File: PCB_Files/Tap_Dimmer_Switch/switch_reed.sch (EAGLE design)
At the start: 37 parts, among them P1 HT7333

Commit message: Added Design with additional reed (magnet) sensor
this version is not entirely finished and has to be improved upon
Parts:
- added C4, C6: 10nF, rcl:C-EUC0805
- added C7: 100u, rcl:CPOL-EUE5-8.5
- added R16, R17, R18, R19, R20, R22, R23, R25: 200k, rcl:R-EU_R0805
- added R21: 100k, rcl:R-EU_R0805
- added R24: 50k, rcl:R-EU_R0805
- added REED: (no value), jumper:JP1E
- added U$1, U$5, U$7: AO3401, diyHue:P-CH_AO3401
- added U$4, U$6, U$8: IRLML2502, diyHue:N-CH_IRLML2502
- C1: device rcl:C-EU025-025X050 -> rcl:C-EUC0805
- C2, C3: value 10nF -> 100u
- C5: value 100u -> 10u
- R1, R11, R12, R13, R14, R15, R2, R3, R4, R5, R8, R9: device diyHue:R-EU_MULTI -> rcl:R-EU_R0805
- R10: value 4k7 -> 10k; device diyHue:R-EU_MULTI -> rcl:R-EU_R0805
- R6, R7: value 100k -> 200k; device diyHue:R-EU_MULTI -> rcl:R-EU_R0805
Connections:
- removed net N$9: R15.1, U2.RX
- new net ADC: R23.1, R24.2, U2.ADC
- new net ESP_RX: R15.1, R21.1, R25.2, U2.RX
- new net N$11: C6.1, R19.2, U$1.D, U$5.G
- new net N$12: C4.1, R16.2, U$5.D
- new net N$13: C4.2, R17.2, U$4.G
- new net N$14: C6.2, R18.2, U$6.G
- new net N$16: R20.2, U$7.G, U$8.D
- new net N$17: R23.2, U$7.D
- new net N$18: R21.2, REED.1, U$1.G
- net +3V3: no longer R1.2, U$2.S
- net +5V: now also C7.+, R1.2, R20.1, REED.2, U$1.S, U$2.S, U$5.S, U$7.S
- net GND: now also C7.-, R16.1, R17.1, R18.1, R19.1, R22.1, R24.1, R25.1, U$4.S, U$6.S, U$8.S
- net GP0: now also R22.2, U$8.G
- net GP13: now also BTN5.D, R13.2; no longer BTN4.D, R5.2
- net GP14: now also BTN2.D, R3.2; no longer BTN5.D, R13.2
- net GP5: now also BTN4.D, R5.2; no longer BTN2.D, R3.2
- net RST: now also U$4.D, U$6.D
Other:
- moved on the sheet: R8, R9

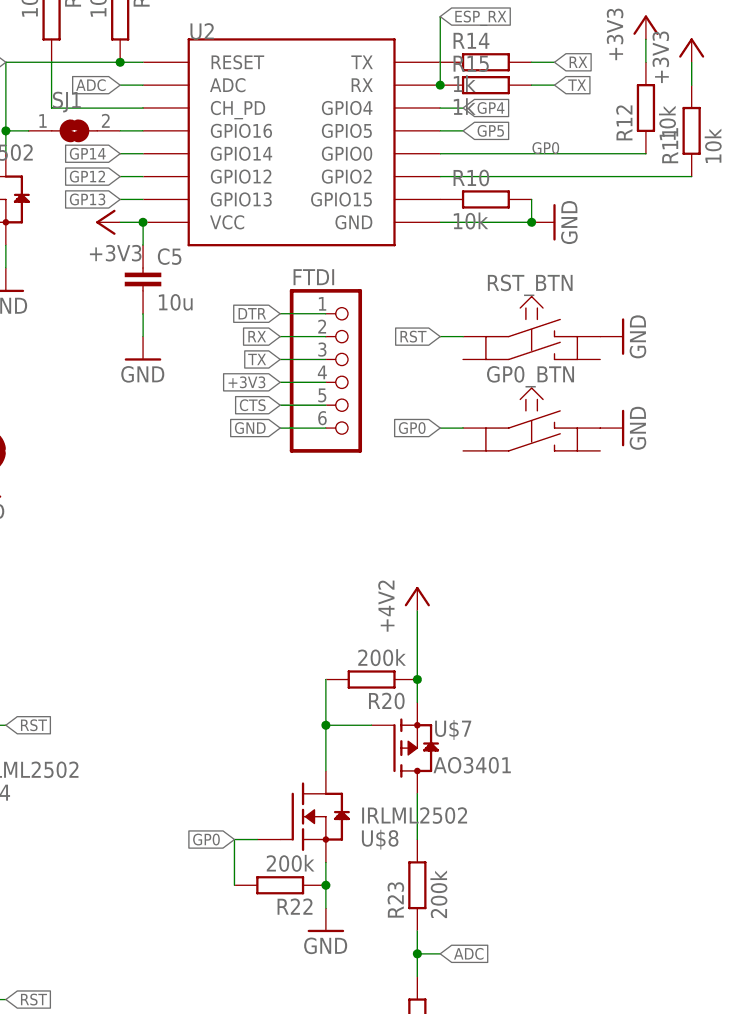
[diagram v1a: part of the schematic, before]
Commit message: created additional compact design of ws2812b module
this new design features smaller footprint, but the esp module ist partially outside the board, which will result in better wifi connection.

additionally the footprint of the HT7333 has been fixed as previously it had used the wrong package.
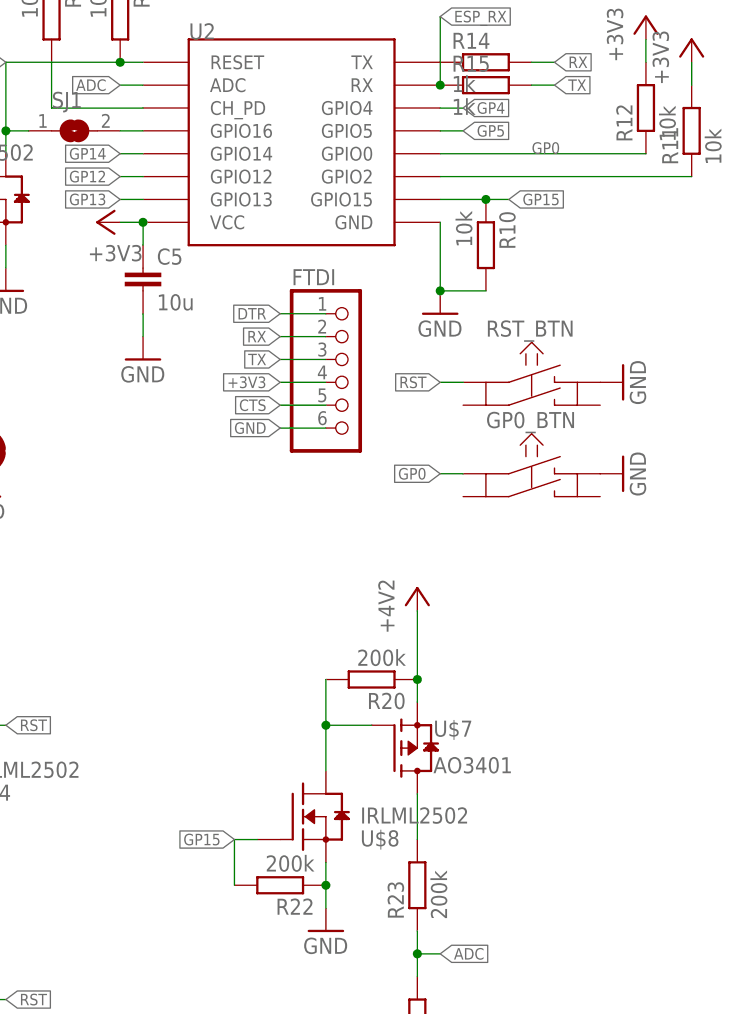
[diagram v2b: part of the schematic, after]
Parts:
- P1: device diyHue:HT7333 -> diyHue:HT7333SOT89
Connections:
- removed net N$4: R10.1, U2.GPIO15
- new net GP15: R10.1, R22.2, U$8.G, U2.GPIO15
- net GP0: no longer R22.2, U$8.G
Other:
- moved on the sheet: GP0_BTN, R10, RST_BTN
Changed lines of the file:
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@@
 <part name="C1" library="rcl" deviceset="C-EU" device="C0805" value="10nF"/>
 <part name="GND9" library="supply1" deviceset="GND" device=""/>
-<part name="P1" library="diyHue" deviceset="HT7333" device=""/>
+<part name="P1" library="diyHue" deviceset="HT7333" device="SOT89" value="HT7333"/>
 <part name="GND10" library="supply1" deviceset="GND" device=""/>
 <part name="FTDI" library="pinhead-2" deviceset="PINHD-1X06" device="_2.54-S"/>
@@
 <instance part="GND6" gate="1" x="83.82" y="0"/>
 <instance part="GND7" gate="1" x="96.52" y="0"/>
-<instance part="GND8" gate="1" x="167.64" y="15.24" rot="R90"/>
-<instance part="R10" gate="G$1" x="160.02" y="17.78"/>
+<instance part="GND8" gate="1" x="154.94" y="5.08"/>
+<instance part="R10" gate="G$1" x="160.02" y="12.7" rot="R270"/>
 <instance part="R11" gate="G$1" x="182.88" y="25.4" rot="R90"/>
 <instance part="R12" gate="G$1" x="177.8" y="27.94" rot="R90"/>
@@
 <instance part="C2" gate="G$1" x="68.58" y="45.72"/>
 <instance part="C3" gate="G$1" x="40.64" y="45.72"/>
-<instance part="RST_BTN" gate="G$1" x="165.1" y="0"/>
+<instance part="RST_BTN" gate="G$1" x="165.1" y="-5.08"/>
 <instance part="+3V4" gate="G$1" x="182.88" y="35.56"/>
-<instance part="GND11" gate="1" x="175.26" y="2.54" rot="R90"/>
-<instance part="GP0_BTN" gate="G$1" x="165.1" y="-10.16"/>
-<instance part="GND12" gate="1" x="175.26" y="-7.62" rot="R90"/>
+<instance part="GND11" gate="1" x="175.26" y="-2.54" rot="R90"/>
+<instance part="GP0_BTN" gate="G$1" x="165.1" y="-15.24"/>
+<instance part="GND12" gate="1" x="175.26" y="-12.7" rot="R90"/>
 <instance part="SJ1" gate="1" x="114.3" y="25.4"/>
 <instance part="R13" gate="G$1" x="66.04" y="2.54" rot="R90"/>
@@
 <pinref part="U2" gate="G$1" pin="GND"/>
 <pinref part="GND8" gate="1" pin="GND"/>
-<wire x1="165.1" y1="15.24" x2="154.94" y2="15.24" width="0.1524" layer="91"/>
+<wire x1="154.94" y1="7.62" x2="154.94" y2="15.24" width="0.1524" layer="91"/>
 <pinref part="R10" gate="G$1" pin="2"/>
-<wire x1="165.1" y1="17.78" x2="165.1" y2="15.24" width="0.1524" layer="91"/>
-<junction x="165.1" y="15.24"/>
+<wire x1="160.02" y1="7.62" x2="154.94" y2="7.62" width="0.1524" layer="91"/>
+<junction x="154.94" y="7.62"/>
 </segment>
 <segment>
@@
 <segment>
 <pinref part="RST_BTN" gate="G$1" pin="A"/>
-<wire x1="157.48" y1="2.54" x2="154.94" y2="2.54" width="0.1524" layer="91"/>
-<label x="154.94" y="2.54" size="1.27" layer="95" rot="R180" xref="yes"/>
+<wire x1="157.48" y1="-2.54" x2="154.94" y2="-2.54" width="0.1524" layer="91"/>
+<label x="154.94" y="-2.54" size="1.27" layer="95" rot="R180" xref="yes"/>
 </segment>
 <segment>
@@
 </segment>
 </net>
-<net name="N$4" class="0">
+<net name="GP15" class="0">
 <segment>
 <pinref part="U2" gate="G$1" pin="GPIO15"/>
 <pinref part="R10" gate="G$1" pin="1"/>
-</segment>
-</net>
-<net name="N$5" class="0">
-<segment>
-<pinref part="U2" gate="G$1" pin="GPIO2"/>
-<pinref part="R11" gate="G$1" pin="1"/>
-<wire x1="154.94" y1="20.32" x2="182.88" y2="20.32" width="0.1524" layer="91"/>
-</segment>
-</net>
-<net name="GP0" class="0">
-<segment>
-<pinref part="R12" gate="G$1" pin="1"/>
-<pinref part="U2" gate="G$1" pin="GPIO0"/>
-<wire x1="177.8" y1="22.86" x2="154.94" y2="22.86" width="0.1524" layer="91"/>
-<label x="165.1" y="22.86" size="1.27" layer="95"/>
-</segment>
-<segment>
-<pinref part="GP0_BTN" gate="G$1" pin="A"/>
-<wire x1="157.48" y1="-7.62" x2="154.94" y2="-7.62" width="0.1524" layer="91"/>
-<label x="154.94" y="-7.62" size="1.27" layer="95" rot="R180" xref="yes"/>
+<wire x1="160.02" y1="17.78" x2="162.56" y2="17.78" width="0.1524" layer="91"/>
+<junction x="160.02" y="17.78"/>
+<label x="162.56" y="17.78" size="1.27" layer="95" xref="yes"/>
+<wire x1="160.02" y1="17.78" x2="154.94" y2="17.78" width="0.1524" layer="91"/>
 </segment>
 <segment>
@@
 </segment>
 </net>
+<net name="N$5" class="0">
+<segment>
+<pinref part="U2" gate="G$1" pin="GPIO2"/>
+<pinref part="R11" gate="G$1" pin="1"/>
+<wire x1="154.94" y1="20.32" x2="182.88" y2="20.32" width="0.1524" layer="91"/>
+</segment>
+</net>
+<net name="GP0" class="0">
+<segment>
+<pinref part="R12" gate="G$1" pin="1"/>
+<pinref part="U2" gate="G$1" pin="GPIO0"/>
+<wire x1="177.8" y1="22.86" x2="154.94" y2="22.86" width="0.1524" layer="91"/>
+<label x="165.1" y="22.86" size="1.27" layer="95"/>
+</segment>
+<segment>
+<pinref part="GP0_BTN" gate="G$1" pin="A"/>
+<wire x1="157.48" y1="-12.7" x2="154.94" y2="-12.7" width="0.1524" layer="91"/>
+<label x="154.94" y="-12.7" size="1.27" layer="95" rot="R180" xref="yes"/>
+</segment>
+</net>
